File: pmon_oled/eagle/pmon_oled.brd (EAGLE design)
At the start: 60 x 60 mm, 30 parts, among them J1 USB, J2 USB, J4 USB_A, J5 PINHD-2X3, Q1 16Mhz, U1 LTC2943, U2 FT232RL, U4 ATMEGA328TQFP32

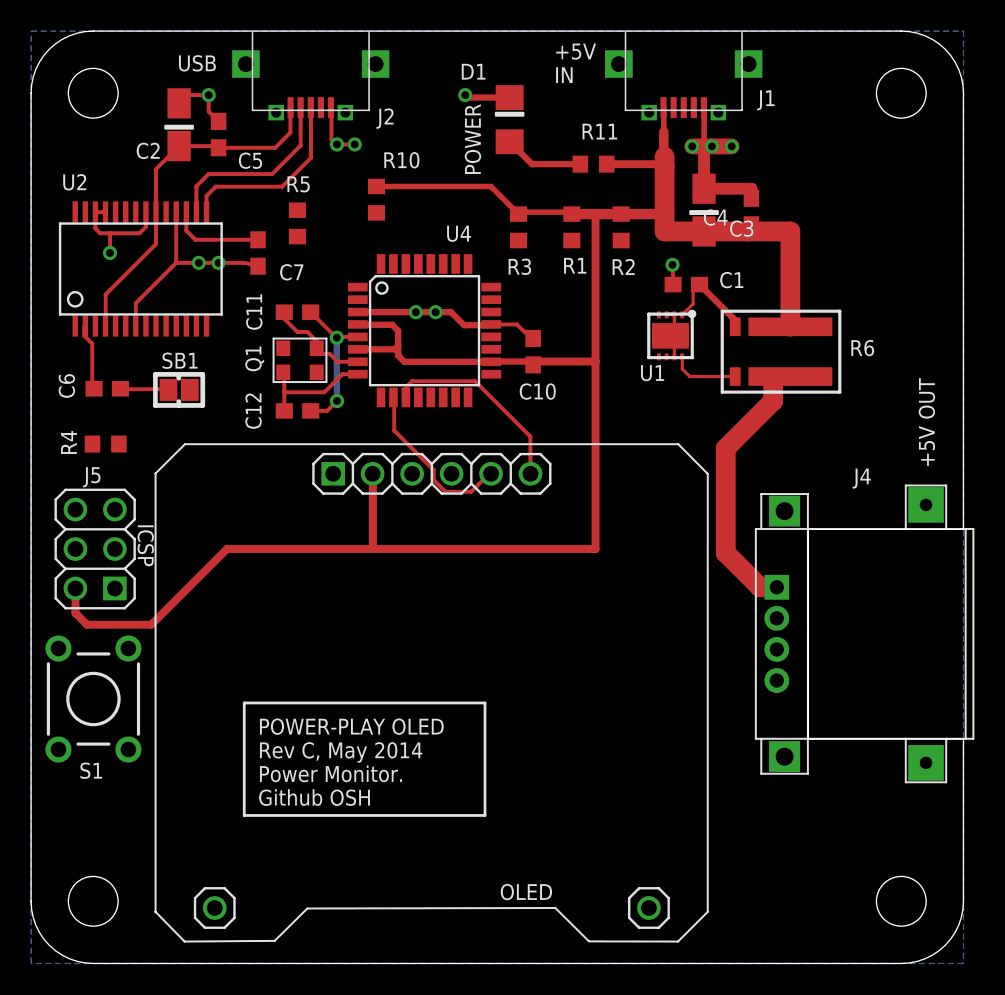
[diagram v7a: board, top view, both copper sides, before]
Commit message: Restoring the pmon_oled design with 3.8V regulator.
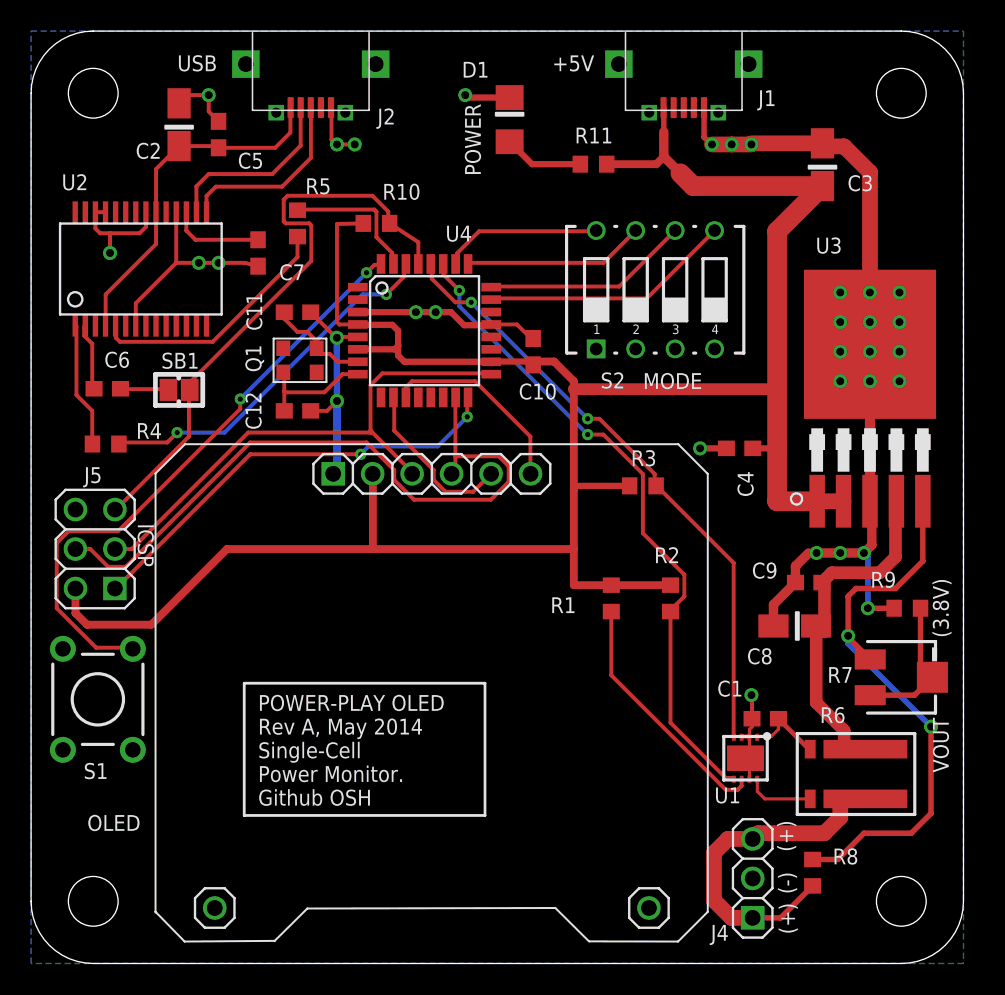
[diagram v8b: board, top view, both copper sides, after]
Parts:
- added C8: 10uF, pmon_oled:A/3216-18R
- added C9: 0.1uF, pmon_oled:C0603
- added R7: 1K, pmon_oled:TRIM-POT_SM-42/43A
- added R8: 8K2 1%, pmon_oled:R0603
- added R9: 3K3 1%, pmon_oled:R0603
- added S2: DIP_SWITCH-X4, pmon_oled:DIP-SWITCH-X4
- added U3: LT1764AEQ, pmon_oled:TO263-5
- J4: value USB_A -> PINHD-1X3; device pmon_oled:USB_A -> pmon_oled:1X03
- moved C1 28.4 mm to (47.2, 15.7)
- moved U1 27.6 mm to (46.0, 13.2)
- moved R6 27.6 mm to (56.4, 12.2)
- moved R2 24.1 mm to (41.1, 23.5)
- moved R1 24.0 mm to (37.3, 23.5)
- moved R3 18.5 mm to (39.4, 30.7), turned to 180 degrees
- moved J4 15.9 mm to (46.4, 5.47)
- moved C4 15.3 mm to (45.6, 33.1), turned to 180 degrees
- moved C3 8.16 mm to (50.9, 51.4)
- moved R10 1.52 mm to (22.2, 47.6), turned to 180 degrees
- moved S1 0.29 mm to (4.30, 17.0)
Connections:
- removed net N$4: J4.2, J4.3
- new net CONFIG1: S2.8, U4.26
- new net CONFIG2: S2.7, U4.25
- new net CONFIG3: S2.6, U4.24
- new net CONFIG4: S2.5, U4.23
- new net N$18: R7.1, R7.2, R9.1
- new net N$19: R7.3, R8.2, U3.5
- new net N$9: C8.+, C9.1, R6.I2, U3.4
- net +5V: now also U3.1, U3.2; no longer R6.I2
- net GND: now also C8.-, C9.2, J4.2, R9.2, S2.1, S2.2, S2.3, S2.4, U3.3, U3.6; no longer J4.4
- net N$22: now also J4.3, R8.1
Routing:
- net GND: track 72.2 -> 121.1 mm, vias 15 -> 32
- net MOSI: track 0.11 -> 43.8 mm
- net I2C-DATA: track 0.00 -> 42.5 mm, vias 0 -> 2
- net I2C-CLK: track 0.13 -> 39.6 mm, vias 0 -> 2
- net START: track 0.00 -> 38.9 mm, vias 0 -> 2
- net RESET: track 0.00 -> 38.6 mm
- net N$19: track 0.00 -> 36.7 mm, vias 0 -> 2
- net SCK: track 0.30 -> 34.7 mm
- net MISO: track 0.12 -> 28.5 mm, vias 0 -> 2
- net SER_RX: track 0.00 -> 23.7 mm, vias 0 -> 2
- net N$9: track 0.00 -> 22.8 mm
- net +5V: track 133.1 -> 155.1 mm
- net CONFIG4: track 0.00 -> 16.2 mm
- net N$8: track 0.00 -> 16.1 mm
- net N$1: track 0.05 -> 16.1 mm
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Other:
- outline, holes or cut-outs redrawn
- board text added: "(+)"
- board text added: "(-)"
- board text added: "(3.8V)"
- board text added: "+5V"
- board text added: "MODE"
- board text added: "POWER-PLAY OLED Rev A, May 2014 Single-Cell Power Monitor. Github OSH"
- board text added: "VOUT"
- board text removed: "+5V IN"
- board text removed: "+5V OUT"
- board text removed: "POWER-PLAY OLED Rev C, May 2014 Power Monitor. Github OSH"
